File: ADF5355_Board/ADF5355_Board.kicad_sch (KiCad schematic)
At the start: 0 parts

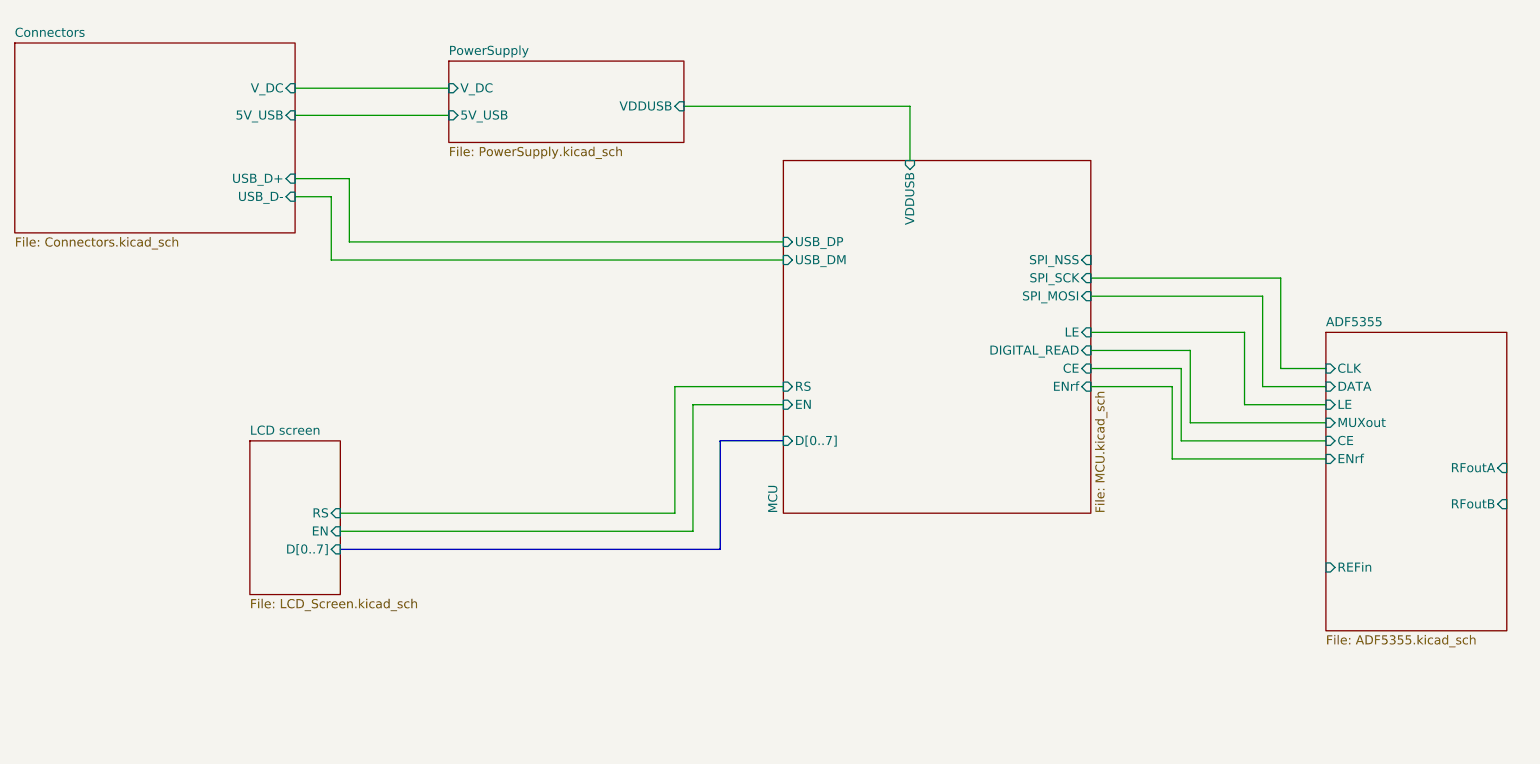
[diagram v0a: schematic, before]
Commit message: Finished MCU board
Finished MCU board and started finishing up the VCO board
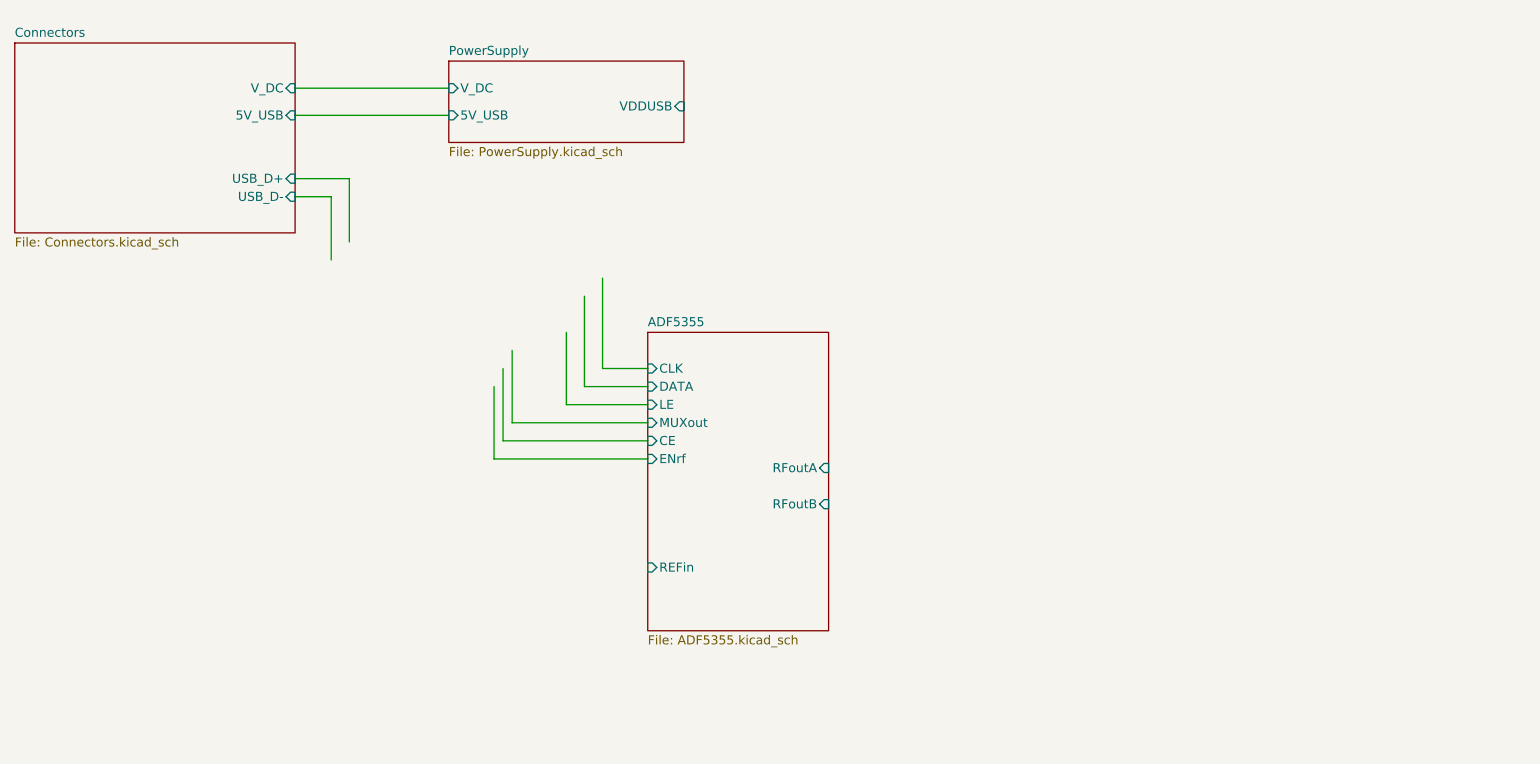
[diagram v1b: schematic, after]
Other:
- removed sheet LCD screen
- removed sheet MCU
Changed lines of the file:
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@@
 (kicad_sch (version 20230121) (generator eeschema)
   (paper "A4")
-  (wire (pts (xy 66.04 96.52) (xy 115.57 96.52))
-    (stroke (width 0) (type default))
-  )
-  (wire (pts (xy 193.04 78.74) (xy 204.47 78.74))
+  (wire (pts (xy 97.79 78.74) (xy 109.22 78.74))
     (stroke (width 0) (type default))
   )
@@
     (stroke (width 0) (type default))
   )
-  (wire (pts (xy 185.42 81.28) (xy 204.47 81.28))
+  (wire (pts (xy 90.17 81.28) (xy 109.22 81.28))
     (stroke (width 0) (type default))
   )
-  (wire (pts (xy 115.57 78.74) (xy 115.57 96.52))
-    (stroke (width 0) (type default))
-  )
-  (wire (pts (xy 182.88 76.2) (xy 182.88 86.36))
+  (wire (pts (xy 87.63 76.2) (xy 87.63 86.36))
     (stroke (width 0) (type default))
   )
@@
     (stroke (width 0) (type default))
   )
-  (wire (pts (xy 66.04 93.98) (xy 113.03 93.98))
+  (wire (pts (xy 100.33 63.5) (xy 100.33 76.2))
     (stroke (width 0) (type default))
   )
-  (wire (pts (xy 195.58 63.5) (xy 195.58 76.2))
+  (wire (pts (xy 88.9 73.66) (xy 88.9 83.82))
     (stroke (width 0) (type default))
   )
-  (wire (pts (xy 64.77 58.42) (xy 128.27 58.42))
+  (wire (pts (xy 90.17 71.12) (xy 90.17 81.28))
     (stroke (width 0) (type default))
   )
-  (wire (pts (xy 184.15 73.66) (xy 184.15 83.82))
-    (stroke (width 0) (type default))
-  )
-  (wire (pts (xy 114.3 36.83) (xy 146.05 36.83))
-    (stroke (width 0) (type default))
-  )
-  (wire (pts (xy 185.42 71.12) (xy 185.42 81.28))
-    (stroke (width 0) (type default))
-  )
-  (wire (pts (xy 67.31 55.88) (xy 128.27 55.88))
-    (stroke (width 0) (type default))
-  )
-  (wire (pts (xy 171.45 73.66) (xy 184.15 73.66))
-    (stroke (width 0) (type default))
-  )
-  (wire (pts (xy 171.45 71.12) (xy 185.42 71.12))
-    (stroke (width 0) (type default))
-  )
-  (wire (pts (xy 184.15 83.82) (xy 204.47 83.82))
+  (wire (pts (xy 88.9 83.82) (xy 109.22 83.82))
     (stroke (width 0) (type default))
   )
@@
     (stroke (width 0) (type default))
   )
-  (wire (pts (xy 171.45 76.2) (xy 182.88 76.2))
+  (wire (pts (xy 102.87 73.66) (xy 102.87 60.96))
     (stroke (width 0) (type default))
   )
-  (wire (pts (xy 113.03 76.2) (xy 113.03 93.98))
-    (stroke (width 0) (type default))
-  )
-  (wire (pts (xy 198.12 73.66) (xy 198.12 60.96))
-    (stroke (width 0) (type default))
-  )
-  (bus (pts (xy 119.38 83.82) (xy 119.38 99.06))
-    (stroke (width 0) (type default))
-  )
-  (wire (pts (xy 171.45 68.58) (xy 193.04 68.58))
-    (stroke (width 0) (type default))
-  )
-  (wire (pts (xy 128.27 78.74) (xy 115.57 78.74))
-    (stroke (width 0) (type default))
-  )
-  (wire (pts (xy 182.88 86.36) (xy 204.47 86.36))
+  (wire (pts (xy 87.63 86.36) (xy 109.22 86.36))
     (stroke (width 0) (type default))
   )
@@
     (stroke (width 0) (type default))
   )
-  (wire (pts (xy 171.45 63.5) (xy 195.58 63.5))
+  (wire (pts (xy 100.33 76.2) (xy 109.22 76.2))
     (stroke (width 0) (type default))
   )
-  (wire (pts (xy 195.58 76.2) (xy 204.47 76.2))
+  (wire (pts (xy 102.87 73.66) (xy 109.22 73.66))
     (stroke (width 0) (type default))
   )
-  (wire (pts (xy 128.27 76.2) (xy 113.03 76.2))
-    (stroke (width 0) (type default))
-  )
-  (wire (pts (xy 198.12 73.66) (xy 204.47 73.66))
-    (stroke (width 0) (type default))
-  )
-  (bus (pts (xy 128.27 83.82) (xy 119.38 83.82))
-    (stroke (width 0) (type default))
-  )
-  (wire (pts (xy 193.04 68.58) (xy 193.04 78.74))
-    (stroke (width 0) (type default))
-  )
-  (bus (pts (xy 66.04 99.06) (xy 119.38 99.06))
-    (stroke (width 0) (type default))
-  )
-  (wire (pts (xy 171.45 60.96) (xy 198.12 60.96))
-    (stroke (width 0) (type default))
-  )
-  (wire (pts (xy 146.05 36.83) (xy 146.05 44.45))
+  (wire (pts (xy 97.79 68.58) (xy 97.79 78.74))
     (stroke (width 0) (type default))
   )
@@
       (project "ADF5355_Board"
         (path "/29349b68-071c-451b-9b1e-10b5ef7e12a6" (page "2"))
-      )
-    )
-  )
-  (sheet (at 128.27 44.45) (size 43.18 49.53) (fields_autoplaced)
-    (stroke (width 0.1524) (type solid))
-    (fill (color 0 0 0 0.0000))
-    (property "Sheetname" "MCU" (at 127.5584 93.98 90)
-      (effects (font (size 1.27 1.27)) (justify left bottom))
-    )
-    (property "Sheetfile" "MCU.kicad_sch" (at 172.0346 93.98 90)
-      (effects (font (size 1.27 1.27)) (justify left top))
-    )
-    (pin "VDDUSB" input (at 146.05 44.45 90)
-      (effects (font (size 1.27 1.27)) (justify right))
-    )
-    (pin "D[0..7]" input (at 128.27 83.82 180)
-      (effects (font (size 1.27 1.27)) (justify left))
-    )
-    (pin "SPI_NSS" input (at 171.45 58.42 0)
-      (effects (font (size 1.27 1.27)) (justify right))
-    )
-    (pin "SPI_SCK" input (at 171.45 60.96 0)
-      (effects (font (size 1.27 1.27)) (justify right))
-    )
-    (pin "SPI_MOSI" input (at 171.45 63.5 0)
-      (effects (font (size 1.27 1.27)) (justify right))
-    )
-    (pin "USB_DM" input (at 128.27 58.42 180)
-      (effects (font (size 1.27 1.27)) (justify left))
-    )
-    (pin "USB_DP" input (at 128.27 55.88 180)
-      (effects (font (size 1.27 1.27)) (justify left))
-    )
-    (pin "RS" input (at 128.27 76.2 180)
-      (effects (font (size 1.27 1.27)) (justify left))
-    )
-    (pin "EN" input (at 128.27 78.74 180)
-      (effects (font (size 1.27 1.27)) (justify left))
-    )
-    (pin "DIGITAL_READ" input (at 171.45 71.12 0)
-      (effects (font (size 1.27 1.27)) (justify right))
-    )
-    (pin "LE" input (at 171.45 68.58 0)
-      (effects (font (size 1.27 1.27)) (justify right))
-    )
-    (pin "CE" input (at 171.45 73.66 0)
-      (effects (font (size 1.27 1.27)) (justify right))
-    )
-    (pin "ENrf" input (at 171.45 76.2 0)
-      (effects (font (size 1.27 1.27)) (justify right))
-    )
-    (instances
-      (project "ADF5355_Board"
-        (path "/29349b68-071c-451b-9b1e-10b5ef7e12a6" (page "3"))
       )
     )
@@
     )
   )
-  (sheet (at 204.47 68.58) (size 25.4 41.91) (fields_autoplaced)
+  (sheet (at 109.22 68.58) (size 25.4 41.91) (fields_autoplaced)
     (stroke (width 0.1524) (type solid))
     (fill (color 0 0 0 0.0000))
-    (property "Sheetname" "ADF5355" (at 204.47 67.8684 0)
+    (property "Sheetname" "ADF5355" (at 109.22 67.8684 0)
       (effects (font (size 1.27 1.27)) (justify left bottom))
     )
-    (property "Sheetfile" "ADF5355.kicad_sch" (at 204.47 111.0746 0)
+    (property "Sheetfile" "ADF5355.kicad_sch" (at 109.22 111.0746 0)
       (effects (font (size 1.27 1.27)) (justify left top))
     )
-    (pin "ENrf" input (at 204.47 86.36 180)
+    (pin "ENrf" input (at 109.22 86.36 180)
       (effects (font (size 1.27 1.27)) (justify left))
     )
-    (pin "CE" input (at 204.47 83.82 180)
+    (pin "CE" input (at 109.22 83.82 180)
       (effects (font (size 1.27 1.27)) (justify left))
     )
-    (pin "MUXout" input (at 204.47 81.28 180)
+    (pin "MUXout" input (at 109.22 81.28 180)
       (effects (font (size 1.27 1.27)) (justify left))
     )
-    (pin "LE" input (at 204.47 78.74 180)
+    (pin "LE" input (at 109.22 78.74 180)
       (effects (font (size 1.27 1.27)) (justify left))
     )
-    (pin "DATA" input (at 204.47 76.2 180)
+    (pin "DATA" input (at 109.22 76.2 180)
       (effects (font (size 1.27 1.27)) (justify left))
     )
-    (pin "CLK" input (at 204.47 73.66 180)
+    (pin "CLK" input (at 109.22 73.66 180)
       (effects (font (size 1.27 1.27)) (justify left))
     )
-    (pin "REFin" input (at 204.47 101.6 180)
+    (pin "REFin" input (at 109.22 101.6 180)
       (effects (font (size 1.27 1.27)) (justify left))
     )
-    (pin "RFoutB" input (at 229.87 92.71 0)
+    (pin "RFoutB" input (at 134.62 92.71 0)
       (effects (font (size 1.27 1.27)) (justify right))
     )
-    (pin "RFoutA" input (at 229.87 87.63 0)
+    (pin "RFoutA" input (at 134.62 87.63 0)
       (effects (font (size 1.27 1.27)) (justify right))
     )
@@
       )
     )
-  )
-  (sheet (at 53.34 83.82) (size 12.7 21.59) (fields_autoplaced)
-    (stroke (width 0.1524) (type solid))
-    (fill (color 0 0 0 0.0000))
-    (property "Sheetname" "LCD screen" (at 53.34 83.1084 0)
-      (effects (font (size 1.27 1.27)) (justify left bottom))
-    )
-    (property "Sheetfile" "LCD_Screen.kicad_sch" (at 53.34 105.9946 0)
-      (effects (font (size 1.27 1.27)) (justify left top))
-    )
-    (property "Field2" "" (at 53.34 83.82 0)
-      (effects (font (size 1.27 1.27)) hide)
-    )
-    (pin "EN" input (at 66.04 96.52 0)
-      (effects (font (size 1.27 1.27)) (justify right))
-    )
-    (pin "RS" input (at 66.04 93.98 0)
-      (effects (font (size 1.27 1.27)) (justify right))
-    )
-    (pin "D[0..7]" input (at 66.04 99.06 0)
-      (effects (font (size 1.27 1.27)) (justify right))
-    )
-    (instances
-      (project "ADF5355_Board"
-        (path "/29349b68-071c-451b-9b1e-10b5ef7e12a6" (page "5"))
-      )
-    )

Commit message: IDK where I stopped
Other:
- sheet ADF5355 ports: added RFin, RFout1, RFout2, RFout3, Vrf; removed REFin, RFoutA, RFoutB
- sheet Connectors ports: added CE, ENrf, LE, MUXout, RFin, RFout1, RFout2, RFout3, SPI_MISO, SPI_MOSI, SPI_NSS, SPI_SCK; removed 5V_USB, USB_D+, USB_D-
- sheet PowerSupply ports: added none; removed 5V_USB, VDDUSB
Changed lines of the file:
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@@
 (kicad_sch (version 20230121) (generator eeschema)
   (paper "A4")
-  (wire (pts (xy 97.79 78.74) (xy 109.22 78.74))
+  (wire (pts (xy 36.83 110.49) (xy 73.66 110.49))
     (stroke (width 0) (type default))
   )
-  (wire (pts (xy 59.69 49.53) (xy 64.77 49.53))
+  (wire (pts (xy 130.81 44.45) (xy 130.81 99.06))
     (stroke (width 0) (type default))
   )
-  (wire (pts (xy 90.17 81.28) (xy 109.22 81.28))
+  (wire (pts (xy 73.66 46.99) (xy 127 46.99))
     (stroke (width 0) (type default))
   )
-  (wire (pts (xy 87.63 76.2) (xy 87.63 86.36))
+  (wire (pts (xy 36.83 66.04) (xy 36.83 110.49))
     (stroke (width 0) (type default))
   )
-  (wire (pts (xy 64.77 49.53) (xy 64.77 58.42))
+  (wire (pts (xy 127 46.99) (xy 127 96.52))
     (stroke (width 0) (type default))
   )
-  (wire (pts (xy 100.33 63.5) (xy 100.33 76.2))
+  (wire (pts (xy 58.42 87.63) (xy 58.42 66.04))
     (stroke (width 0) (type default))
   )
-  (wire (pts (xy 88.9 73.66) (xy 88.9 83.82))
+  (wire (pts (xy 73.66 97.79) (xy 48.26 97.79))
     (stroke (width 0) (type default))
   )
-  (wire (pts (xy 90.17 71.12) (xy 90.17 81.28))
+  (wire (pts (xy 130.81 99.06) (xy 99.06 99.06))
     (stroke (width 0) (type default))
   )
-  (wire (pts (xy 88.9 83.82) (xy 109.22 83.82))
+  (wire (pts (xy 50.8 66.04) (xy 50.8 95.25))
     (stroke (width 0) (type default))
   )
-  (wire (pts (xy 59.69 46.99) (xy 67.31 46.99))
+  (wire (pts (xy 123.19 93.98) (xy 123.19 49.53))
     (stroke (width 0) (type default))
   )
-  (wire (pts (xy 102.87 73.66) (xy 102.87 60.96))
+  (wire (pts (xy 73.66 87.63) (xy 58.42 87.63))
     (stroke (width 0) (type default))
   )
-  (wire (pts (xy 87.63 86.36) (xy 109.22 86.36))
+  (wire (pts (xy 73.66 92.71) (xy 53.34 92.71))
     (stroke (width 0) (type default))
   )
-  (wire (pts (xy 59.69 34.29) (xy 81.28 34.29))
+  (wire (pts (xy 50.8 95.25) (xy 73.66 95.25))
     (stroke (width 0) (type default))
   )
-  (wire (pts (xy 59.69 38.1) (xy 81.28 38.1))
+  (wire (pts (xy 73.66 44.45) (xy 130.81 44.45))
     (stroke (width 0) (type default))
   )
-  (wire (pts (xy 100.33 76.2) (xy 109.22 76.2))
+  (wire (pts (xy 73.66 33.02) (xy 95.25 33.02))
     (stroke (width 0) (type default))
   )
-  (wire (pts (xy 102.87 73.66) (xy 109.22 73.66))
+  (wire (pts (xy 53.34 92.71) (xy 53.34 66.04))
     (stroke (width 0) (type default))
   )
-  (wire (pts (xy 97.79 68.58) (xy 97.79 78.74))
+  (wire (pts (xy 73.66 100.33) (xy 45.72 100.33))
     (stroke (width 0) (type default))
   )
-  (wire (pts (xy 67.31 46.99) (xy 67.31 55.88))
+  (wire (pts (xy 55.88 66.04) (xy 55.88 90.17))
     (stroke (width 0) (type default))
   )
-  (sheet (at 81.28 30.48) (size 33.02 11.43) (fields_autoplaced)
+  (wire (pts (xy 45.72 100.33) (xy 45.72 66.04))
+    (stroke (width 0) (type default))
+  )
+  (wire (pts (xy 127 96.52) (xy 99.06 96.52))
+    (stroke (width 0) (type default))
+  )
+  (wire (pts (xy 55.88 90.17) (xy 73.66 90.17))
+    (stroke (width 0) (type default))
+  )
+  (wire (pts (xy 99.06 93.98) (xy 123.19 93.98))
+    (stroke (width 0) (type default))
+  )
+  (wire (pts (xy 123.19 49.53) (xy 73.66 49.53))
+    (stroke (width 0) (type default))
+  )
+  (wire (pts (xy 48.26 97.79) (xy 48.26 66.04))
+    (stroke (width 0) (type default))
+  )
+  (sheet (at 95.25 29.21) (size 33.02 11.43) (fields_autoplaced)
     (stroke (width 0) (type solid))
     (fill (color 0 0 0 0.0000))
-    (property "Sheetname" "PowerSupply" (at 81.28 29.7684 0)
+    (property "Sheetname" "PowerSupply" (at 95.25 28.4984 0)
       (effects (font (size 1.27 1.27)) (justify left bottom))
     )
-    (property "Sheetfile" "PowerSupply.kicad_sch" (at 81.28 42.4946 0)
+    (property "Sheetfile" "PowerSupply.kicad_sch" (at 95.25 41.2246 0)
       (effects (font (size 1.27 1.27)) (justify left top))
     )
-    (pin "V_DC" input (at 81.28 34.29 180)
+    (pin "V_DC" input (at 95.25 33.02 180)
       (effects (font (size 1.27 1.27)) (justify left))
-    )
-    (pin "5V_USB" input (at 81.28 38.1 180)
-      (effects (font (size 1.27 1.27)) (justify left))
-    )
-    (pin "VDDUSB" input (at 114.3 36.83 0)
-      (effects (font (size 1.27 1.27)) (justify right))
     )
     (instances
@@
     )
   )
-  (sheet (at 20.32 27.94) (size 39.37 26.67) (fields_autoplaced)
+  (sheet (at 34.29 26.67) (size 39.37 39.37) (fields_autoplaced)
     (stroke (width 0.1524) (type solid))
     (fill (color 0 0 0 0.0000))
-    (property "Sheetname" "Connectors" (at 20.32 27.2284 0)
+    (property "Sheetname" "Connectors" (at 34.29 25.9584 0)
       (effects (font (size 1.27 1.27)) (justify left bottom))
     )
-    (property "Sheetfile" "Connectors.kicad_sch" (at 20.32 55.1946 0)
+    (property "Sheetfile" "Connectors.kicad_sch" (at 34.29 66.6246 0)
       (effects (font (size 1.27 1.27)) (justify left top))
     )
-    (pin "V_DC" input (at 59.69 34.29 0)
+    (pin "V_DC" input (at 73.66 33.02 0)
       (effects (font (size 1.27 1.27)) (justify right))
     )
-    (pin "USB_D-" input (at 59.69 49.53 0)
+    (pin "CE" input (at 48.26 66.04 270)
+      (effects (font (size 1.27 1.27)) (justify left))
+    )
+    (pin "ENrf" input (at 45.72 66.04 270)
+      (effects (font (size 1.27 1.27)) (justify left))
+    )
+    (pin "LE" input (at 53.34 66.04 270)
+      (effects (font (size 1.27 1.27)) (justify left))
+    )
+    (pin "MUXout" input (at 50.8 66.04 270)
+      (effects (font (size 1.27 1.27)) (justify left))
+    )
+    (pin "SPI_SCK" input (at 58.42 66.04 270)
+      (effects (font (size 1.27 1.27)) (justify left))
+    )
+    (pin "SPI_NSS" input (at 66.04 66.04 270)
+      (effects (font (size 1.27 1.27)) (justify left))
+    )
+    (pin "SPI_MOSI" input (at 55.88 66.04 270)
+      (effects (font (size 1.27 1.27)) (justify left))
+    )
+    (pin "SPI_MISO" input (at 63.5 66.04 270)
+      (effects (font (size 1.27 1.27)) (justify left))
+    )
+    (pin "RFout1" input (at 73.66 49.53 0)
       (effects (font (size 1.27 1.27)) (justify right))
     )
-    (pin "USB_D+" input (at 59.69 46.99 0)
+    (pin "RFout2" input (at 73.66 46.99 0)
       (effects (font (size 1.27 1.27)) (justify right))
     )
-    (pin "5V_USB" input (at 59.69 38.1 0)
+    (pin "RFout3" input (at 73.66 44.45 0)
       (effects (font (size 1.27 1.27)) (justify right))
+    )
+    (pin "RFin" input (at 36.83 66.04 270)
+      (effects (font (size 1.27 1.27)) (justify left))
     )
     (instances
@@
     )
   )
-  (sheet (at 109.22 68.58) (size 25.4 41.91) (fields_autoplaced)
+  (sheet (at 73.66 82.55) (size 25.4 41.91) (fields_autoplaced)
     (stroke (width 0.1524) (type solid))
     (fill (color 0 0 0 0.0000))
-    (property "Sheetname" "ADF5355" (at 109.22 67.8684 0)
+    (property "Sheetname" "ADF5355" (at 73.66 81.8384 0)
       (effects (font (size 1.27 1.27)) (justify left bottom))
     )
-    (property "Sheetfile" "ADF5355.kicad_sch" (at 109.22 111.0746 0)
+    (property "Sheetfile" "ADF5355.kicad_sch" (at 73.66 125.0446 0)
       (effects (font (size 1.27 1.27)) (justify left top))
     )
-    (pin "ENrf" input (at 109.22 86.36 180)
+    (pin "ENrf" input (at 73.66 100.33 180)
       (effects (font (size 1.27 1.27)) (justify left))
     )
-    (pin "CE" input (at 109.22 83.82 180)
+    (pin "CE" input (at 73.66 97.79 180)
       (effects (font (size 1.27 1.27)) (justify left))
     )
-    (pin "MUXout" input (at 109.22 81.28 180)
+    (pin "MUXout" input (at 73.66 95.25 180)
       (effects (font (size 1.27 1.27)) (justify left))
     )
-    (pin "LE" input (at 109.22 78.74 180)
+    (pin "LE" input (at 73.66 92.71 180)
       (effects (font (size 1.27 1.27)) (justify left))
     )
-    (pin "DATA" input (at 109.22 76.2 180)
+    (pin "DATA" input (at 73.66 90.17 180)
       (effects (font (size 1.27 1.27)) (justify left))
     )
-    (pin "CLK" input (at 109.22 73.66 180)
+    (pin "CLK" input (at 73.66 87.63 180)
       (effects (font (size 1.27 1.27)) (justify left))
     )
-    (pin "REFin" input (at 109.22 101.6 180)
+    (pin "Vrf" input (at 91.44 82.55 90)
+      (effects (font (size 1.27 1.27)) (justify right))
+    )
+    (pin "RFout1" input (at 99.06 93.98 0)
+      (effects (font (size 1.27 1.27)) (justify right))
+    )
+    (pin "RFout3" input (at 99.06 99.06 0)
+      (effects (font (size 1.27 1.27)) (justify right))
+    )
+    (pin "RFout2" input (at 99.06 96.52 0)
+      (effects (font (size 1.27 1.27)) (justify right))
+    )
+    (pin "RFin" input (at 73.66 110.49 180)
       (effects (font (size 1.27 1.27)) (justify left))
     )
-    (pin "RFoutB" input (at 134.62 92.71 0)
-      (effects (font (size 1.27 1.27)) (justify right))
-    )
-    (pin "RFoutA" input (at 134.62 87.63 0)
-      (effects (font (size 1.27 1.27)) (justify right))
-    )
     (instances
